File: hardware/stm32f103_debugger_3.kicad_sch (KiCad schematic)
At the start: 18 parts, among them J1 GMSB0531112YEU, J2 Conn_01x06, SW1 SW TACT-SPST, U1 STM32F103CBT6, Y1 ABM8G-8.000MHZ-18-D2Y-T

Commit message: Organize schematic
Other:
- note added: "Debugger"
- note added: "JTAG"
- note added: "Oscilator"
- note added: "USB Mini B"
- note added: "VBAT - C6"
- note added: "VDD1 - C5"
- note added: "VDD2 - C4"
- note added: "VDD3 - C2, 3"
- note added: "VDDA - C7, 8"
- note removed: "VBAT - C15"
- note removed: "VDD1 - C14"
- note removed: "VDD2 - C13"
- note removed: "VDD3 - C11, 12"
- note removed: "VDDA - C16, 17"
- moved on the sheet: C1, C10, C2, C3, C4, C5, C6, C7, C8, C9, J1, J2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

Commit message: Link footprints to Symbols
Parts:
- C1, C10, C2, C3, C4, C5, C6, C7, C8, C9: footprint (none) -> STM32F407 Dev Kit Library:C_0805_2012Metric_Pad1.18x1.45mm_HandSolder
- J1: footprint Package_DFN_QFN:WDFN-10-1EP_3x3mm_P0.5mm_EP1.8x2.5mm -> STM32F407 Dev Kit Library:USB_Mini-B_Wuerth_65100516121_Horizontal
- J2: footprint (none) -> STM32F407 Dev Kit Library:PinHeader_1x06_P2.54mm_Vertical
- R1, R2, R3: footprint (none) -> STM32F407 Dev Kit Library:R_0805_2012Metric_Pad1.20x1.40mm_HandSolder
- SW1: footprint Button_Switch_SMD:Nidec_Copal_CAS-120A -> STM32F407 Dev Kit Library:SW_Push_1P1T_NO_CK_KSC9xxG
- U1: footprint Package_QFP:LQFP-48_7x7mm_P0.5mm -> STM32F407 Dev Kit Library:LQFP-48_7x7mm_P0.5mm
- Y1: footprint (none) -> STM32F407 Dev Kit Library:Crystal_SMD_3225-4Pin_3.2x2.5mm_HandSoldering
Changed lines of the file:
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@@
 			)
 		)
-		(property "Footprint" ""
+		(property "Footprint" "STM32F407 Dev Kit Library:C_0805_2012Metric_Pad1.18x1.45mm_HandSolder"
 			(at 172.4152 55.88 0)
 			(hide yes)
@@
 			)
 		)
-		(property "Footprint" ""
+		(property "Footprint" "STM32F407 Dev Kit Library:R_0805_2012Metric_Pad1.20x1.40mm_HandSolder"
 			(at 212.852 97.79 90)
 			(hide yes)
@@
 			)
 		)
-		(property "Footprint" ""
+		(property "Footprint" "STM32F407 Dev Kit Library:C_0805_2012Metric_Pad1.18x1.45mm_HandSolder"
 			(at 134.3152 63.5 0)
 			(hide yes)
@@
 			)
 		)
-		(property "Footprint" ""
+		(property "Footprint" "STM32F407 Dev Kit Library:PinHeader_1x06_P2.54mm_Vertical"
 			(at 246.38 140.97 0)
 			(hide yes)
@@
 			)
 		)
-		(property "Footprint" ""
+		(property "Footprint" "STM32F407 Dev Kit Library:C_0805_2012Metric_Pad1.18x1.45mm_HandSolder"
 			(at 234.95 43.4848 0)
 			(hide yes)
@@
 			)
 		)
-		(property "Footprint" "Package_QFP:LQFP-48_7x7mm_P0.5mm"
+		(property "Footprint" "STM32F407 Dev Kit Library:LQFP-48_7x7mm_P0.5mm"
 			(at 67.31 140.97 0)
 			(hide yes)
@@
 			)
 		)
-		(property "Footprint" ""
+		(property "Footprint" "STM32F407 Dev Kit Library:C_0805_2012Metric_Pad1.18x1.45mm_HandSolder"
 			(at 121.6152 66.04 0)
 			(hide yes)
@@
 			)
 		)
-		(property "Footprint" ""
+		(property "Footprint" "STM32F407 Dev Kit Library:C_0805_2012Metric_Pad1.18x1.45mm_HandSolder"
 			(at 159.7152 58.42 0)
 			(hide yes)
@@
 			)
 		)
-		(property "Footprint" ""
+		(property "Footprint" "STM32F407 Dev Kit Library:C_0805_2012Metric_Pad1.18x1.45mm_HandSolder"
 			(at 32.7152 77.47 0)
 			(hide yes)
@@
 			)
 		)
-		(property "Footprint" ""
+		(property "Footprint" "STM32F407 Dev Kit Library:C_0805_2012Metric_Pad1.18x1.45mm_HandSolder"
 			(at 187.6552 55.88 0)
 			(hide yes)
@@
 			)
 		)
-		(property "Footprint" "Package_DFN_QFN:WDFN-10-1EP_3x3mm_P0.5mm_EP1.8x2.5mm"
+		(property "Footprint" "STM32F407 Dev Kit Library:USB_Mini-B_Wuerth_65100516121_Horizontal"
 			(at 241.3 100.33 0)
 			(hide yes)
@@
 			)
 		)
-		(property "Footprint" ""
+		(property "Footprint" "STM32F407 Dev Kit Library:R_0805_2012Metric_Pad1.20x1.40mm_HandSolder"
 			(at 40.132 81.28 90)
 			(hide yes)
@@
 			)
 		)
-		(property "Footprint" ""
+		(property "Footprint" "STM32F407 Dev Kit Library:C_0805_2012Metric_Pad1.18x1.45mm_HandSolder"
 			(at 147.0152 60.96 0)
 			(hide yes)
@@
 			)
 		)
-		(property "Footprint" ""
+		(property "Footprint" "STM32F407 Dev Kit Library:R_0805_2012Metric_Pad1.20x1.40mm_HandSolder"
 			(at 50.038 132.08 90)
 			(hide yes)
@@
 			)
 		)
-		(property "Footprint" "Button_Switch_SMD:Nidec_Copal_CAS-120A"
+		(property "Footprint" "STM32F407 Dev Kit Library:SW_Push_1P1T_NO_CK_KSC9xxG"
 			(at 16.51 74.93 0)
 			(hide yes)
@@
 			)
 		)
-		(property "Footprint" ""
+		(property "Footprint" "STM32F407 Dev Kit Library:C_0805_2012Metric_Pad1.18x1.45mm_HandSolder"
 			(at 234.95 53.6448 0)
 			(hide yes)
@@
 			)
 		)
-		(property "Footprint" ""
+		(property "Footprint" "STM32F407 Dev Kit Library:C_0805_2012Metric_Pad1.18x1.45mm_HandSolder"
 			(at 108.9152 66.04 0)
 			(hide yes)
@@
 			)
 		)
-		(property "Footprint" ""
+		(property "Footprint" "STM32F407 Dev Kit Library:Crystal_SMD_3225-4Pin_3.2x2.5mm_HandSoldering"
 			(at 238.76 49.53 0)
 			(hide yes)

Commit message: Convert Schematic to PCB
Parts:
- removed SW1: SW TACT-SPST, STM32F407 Dev Kit Library:SW_Push_1P1T_NO_CK_KSC9xxG, symbol Switch:SW_MEC_5G
- removed Y1: ABM8G-8.000MHZ-18-D2Y-T, STM32F407 Dev Kit Library:Crystal_SMD_3225-4Pin_3.2x2.5mm_HandSoldering, symbol Device:Crystal
- added SW1: SW TACT-SPST, STM32F407 Dev Kit Library:SW_Push_SPST_NO_Alps_SKRK, symbol Switch:SW_Push
- added Y1: ABM8G-8.000MHZ-18-D2Y-T, STM32F407 Dev Kit Library:Crystal_SMD_3225-4Pin_3.2x2.5mm_HandSoldering, symbol Device:Crystal_GND24
- renumbered C7 to C10, C8 to C6, C9 to C7, C10 to C8, C6 to C9
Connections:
- net F103_NRST: now also SW1.2
- net F103_OSC_IN: now also Y1.1
- net F103_OSC_OUT: now also Y1.3
- net GND: now also SW1.1, Y1.2 (G), Y1.4 (G)
- no-connect marks 2 -> 25

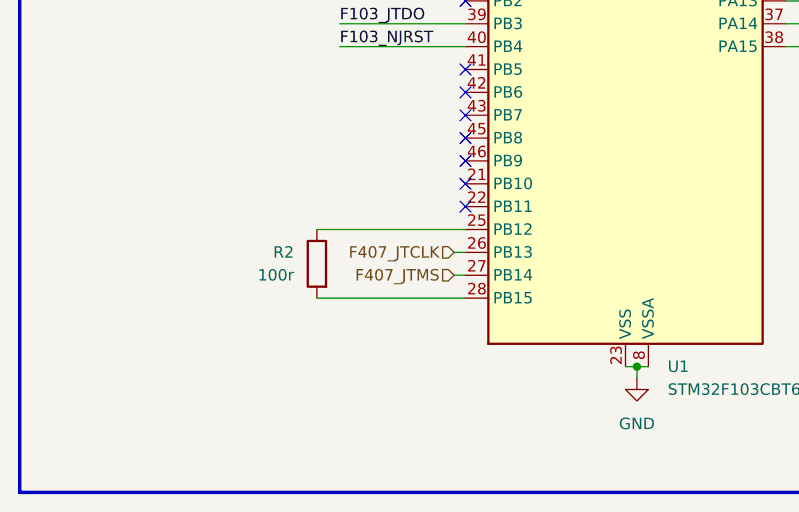
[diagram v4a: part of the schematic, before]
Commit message: Place components for STM32F103 Programmer/Debugger
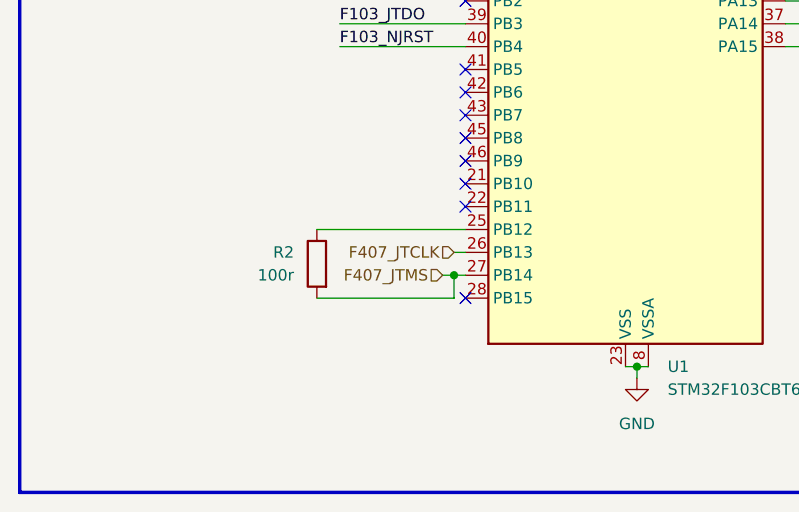
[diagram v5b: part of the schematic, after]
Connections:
- net F407_JTMS: now also R2.2
- net at U1.28 (PB15): no longer R2.2
- no-connect marks 25 -> 26
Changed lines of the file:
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@@
+	)
+	(junction
+		(at 63.5 133.35)
+		(diameter 0)
+		(color 0 0 0 0)
 	)
 	(junction
@@
 	)
 	(no_connect
+		(at 64.77 135.89)
+	)
+	(no_connect
 		(at 64.77 125.73)
 	)
@@
 	(wire
 		(pts
+			(xy 63.5 135.89) (xy 63.5 133.35)
+		)
+		(stroke
+			(width 0)
+			(type default)
+		)
+	)
+	(wire
+		(pts
 			(xy 87.63 53.34) (xy 87.63 55.88)
 		)
@@
 	(wire
 		(pts
+			(xy 63.5 133.35) (xy 64.77 133.35)
+		)
+		(stroke
+			(width 0)
+			(type default)
+		)
+	)
+	(wire
+		(pts
 			(xy 222.25 44.45) (xy 222.25 49.53)
 		)
@@
 	(wire
 		(pts
-			(xy 63.5 133.35) (xy 64.77 133.35)
+			(xy 62.23 133.35) (xy 63.5 133.35)
+		)
+		(stroke
+			(width 0)
+			(type default)
+		)
+	)
+	(wire
+		(pts
+			(xy 48.26 135.89) (xy 63.5 135.89)
 		)
 		(stroke
@@
 		(pts
 			(xy 171.45 48.26) (xy 186.69 48.26)
-		)
-		(stroke
-			(width 0)
-			(type default)
-		)
-	)
-	(wire
-		(pts
-			(xy 64.77 135.89) (xy 48.26 135.89)
 		)
 		(stroke
@@
 	(hierarchical_label "F407_JTMS"
 		(shape input)
-		(at 63.5 133.35 180)
-		(effects
-			(font
+		(at 62.23 133.35 180)
+		(effects
+			(font

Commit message: Route Ethernet section and add global labels
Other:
- moved on the sheet: R2
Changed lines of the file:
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@@
-	)
-	(junction
-		(at 63.5 133.35)
-		(diameter 0)
-		(color 0 0 0 0)
 	)
 	(junction
@@
 	(wire
 		(pts
-			(xy 62.23 133.35) (xy 63.5 133.35)
-		)
-		(stroke
-			(width 0)
-			(type default)
-		)
-	)
-	(wire
-		(pts
-			(xy 48.26 135.89) (xy 63.5 135.89)
+			(xy 46.99 135.89) (xy 63.5 135.89)
 		)
 		(stroke
@@
 	(wire
 		(pts
-			(xy 48.26 128.27) (xy 64.77 128.27)
+			(xy 46.99 128.27) (xy 64.77 128.27)
 		)
 		(stroke
@@
 		)
 	)
-	(hierarchical_label "F407_NTRST"
+	(global_label "F407_NTRST"
 		(shape input)
 		(at 63.5 97.79 180)
+		(fields_autoplaced yes)
 		(effects
 			(font
@@
 			(justify right)
 		)
-	)
-	(hierarchical_label "F407_JTCLK"
+		(property "Intersheetrefs" "${INTERSHEET_REFS}"
+			(at 49.0849 97.79 0)
+			(hide yes)
+			(show_name no)
+			(do_not_autoplace no)
+			(effects
+				(font
+					(size 1.27 1.27)
+				)
+				(justify right)
+			)
+		)
+	)
+	(global_label "F407_JTCLK"
 		(shape input)
 		(at 63.5 130.81 180)
+		(fields_autoplaced yes)
 		(effects
 			(font
@@
 			(justify right)
 		)
-	)
-	(hierarchical_label "F407_JTMS"
+		(property "Intersheetrefs" "${INTERSHEET_REFS}"
+			(at 49.3268 130.81 0)
+			(hide yes)
+			(show_name no)
+			(do_not_autoplace no)
+			(effects
+				(font
+					(size 1.27 1.27)
+				)
+				(justify right)
+			)
+		)
+	)
+	(global_label "F407_JTMS"
 		(shape input)
-		(at 62.23 133.35 180)
+		(at 63.5 133.35 180)
+		(fields_autoplaced yes)
 		(effects
 			(font
@@
 			)
 			(justify right)
+		)
+		(property "Intersheetrefs" "${INTERSHEET_REFS}"
+			(at 50.234 133.35 0)
+			(hide yes)
+			(show_name no)
+			(do_not_autoplace no)
+			(effects
+				(font
+					(size 1.27 1.27)
+				)
+				(justify right)
+			)
 		)
 	)
@@
 	(symbol
 		(lib_id "Device:R")
-		(at 48.26 132.08 0)
+		(at 46.99 132.08 0)
 		(mirror y)
 		(unit 1)
@@
 		(fields_autoplaced yes)
 		(property "Reference" "R2"
-			(at 45.72 130.8099 0)
+			(at 44.45 130.8099 0)
 			(show_name no)
 			(do_not_autoplace no)
@@
 		)
 		(property "Value" "100r"
-			(at 45.72 133.3499 0)
+			(at 44.45 133.3499 0)
 			(show_name no)
 			(do_not_autoplace no)
@@
 		)
 		(property "Footprint" "STM32F407 Dev Kit Library:R_0805_2012Metric_Pad1.20x1.40mm_HandSolder"
-			(at 50.038 132.08 90)
+			(at 48.768 132.08 90)
 			(hide yes)
 			(show_name no)
@@
 		)
 		(property "Datasheet" ""
-			(at 48.26 132.08 0)
+			(at 46.99 132.08 0)
 			(hide yes)
 			(show_name no)
@@
 		)
 		(property "Description" "Resistor"
-			(at 48.26 132.08 0)
-			(hide yes)
-			(show_name no)
+			(at 46.99 132.08 0)
+			(hide yes)
+			(show_name no)

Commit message: Fix typo for C4
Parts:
- C4: value 100nn -> 100n
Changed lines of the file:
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@@
 			)
 		)
-		(property "Value" "100nn"
+		(property "Value" "100n"
 			(at 137.16 60.9599 0)
 			(show_name no)
